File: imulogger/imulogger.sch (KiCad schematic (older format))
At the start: 23 parts, among them J1 DEBUG, J2 BATCONN, J3 CHGCONN, J4 Micro_SD_Card, SW1 SW_SPDT, U1 ESP32-WROOM-32, U2 USFS, U3 MCP1826S

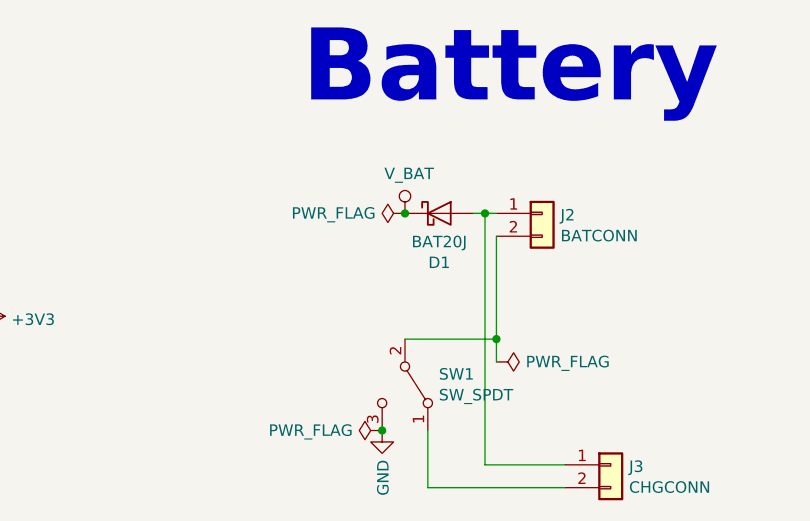
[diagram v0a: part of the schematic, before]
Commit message: make switch route V_BAT instead of GND
even though it shouldn't make a difference it's probably better to
not connect the system load to the charger.
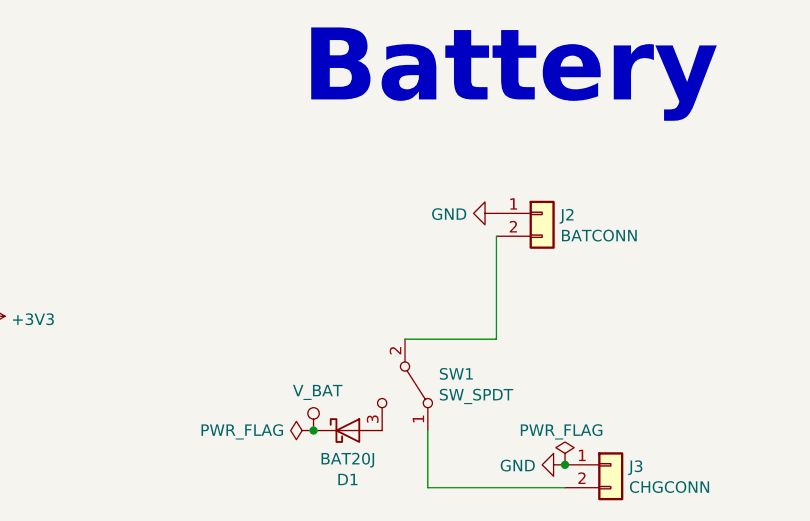
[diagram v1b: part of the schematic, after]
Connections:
- net GND: now also J2.1 (Pin_1), J3.1 (Pin_1); no longer SW1.3 (C)
- new net: D1.2 (A), SW1.3 (C)
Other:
- moved on the sheet: D1
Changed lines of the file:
@@
 $EndComp
-$Comp
-L imulogger-symbols:V_BAT #PWR014
-U 1 1 5CDD3FAE
-P 4350 6450
-F 0 "#PWR014" H 4350 6300 50  0001 C CNN
-F 1 "V_BAT" H 4368 6623 50  0000 C CNN
-F 2 "" H 4350 6450 50  0001 C CNN
-F 3 "" H 4350 6450 50  0001 C CNN
-	1    4350 6450
-	1    0    0    -1
-$EndComp
-Wire Wire Line
-	4750 6550 4750 7000
 $Comp
 L power:GND #PWR013
 U 1 1 5CDF671F
-P 4250 7400
-F 0 "#PWR013" H 4250 7150 50  0001 C CNN
-F 1 "GND" V 4255 7272 50  0000 R CNN
-F 2 "" H 4250 7400 50  0001 C CNN
-F 3 "" H 4250 7400 50  0001 C CNN
-	1    4250 7400
-	1    0    0    -1
-$EndComp
-$Comp
-L power:PWR_FLAG #FLG0105
-U 1 1 5CE03E12
-P 4750 7100
-F 0 "#FLG0105" H 4750 7175 50  0001 C CNN
-F 1 "PWR_FLAG" V 4750 7228 50  0000 L CNN
-F 2 "" H 4750 7100 50  0001 C CNN
-F 3 "~" H 4750 7100 50  0001 C CNN
-	1    4750 7100
+P 4750 6450
+F 0 "#PWR013" H 4750 6200 50  0001 C CNN
+F 1 "GND" V 4755 6322 50  0000 R CNN
+F 2 "" H 4750 6450 50  0001 C CNN
+F 3 "" H 4750 6450 50  0001 C CNN
+	1    4750 6450
 	0    1    1    0
 $EndComp
@@
 L Device:D_Schottky D1
 U 1 1 5CE2A47D
-P 4500 6450
-F 0 "D1" H 4500 6234 50  0000 C CNN
-F 1 "BAT20J" H 4500 6325 50  0000 C CNN
-F 2 "Diode_SMD:D_SOD-323" H 4500 6450 50  0001 C CNN
-F 3 "~" H 4500 6450 50  0001 C CNN
-	1    4500 6450
+P 4100 7400
+F 0 "D1" H 4100 7184 50  0000 C CNN
+F 1 "BAT20J" H 4100 7275 50  0000 C CNN
+F 2 "Diode_SMD:D_SOD-323" H 4100 7400 50  0001 C CNN
+F 3 "~" H 4100 7400 50  0001 C CNN
+	1    4100 7400
 	1    0    0    -1
 $EndComp
@@
 Wire Wire Line
 	4350 7000 4750 7000
-Connection ~ 4750 7000
-Wire Wire Line
-	4750 7000 4750 7100
 $Comp
 L Connector_Generic:Conn_01x02 J3
@@
 Wire Wire Line
 	4450 7650 4450 7400
-Wire Wire Line
-	4650 6450 4700 6450
-Wire Wire Line
-	5050 7550 4700 7550
-Wire Wire Line
-	4700 7550 4700 6450
-Connection ~ 4700 6450
-Wire Wire Line
-	4700 6450 4750 6450
 Text Notes 3900 6000 0    315  ~ 63
 Battery
 $Comp
-L power:PWR_FLAG #FLG0101
-U 1 1 5CE43E5A
-P 4350 6450
-F 0 "#FLG0101" H 4350 6525 50  0001 C CNN
-F 1 "PWR_FLAG" V 4350 6578 50  0000 L CNN
-F 2 "" H 4350 6450 50  0001 C CNN
-F 3 "~" H 4350 6450 50  0001 C CNN
-	1    4350 6450
-	0    -1   -1   0
+L imulogger-symbols:V_BAT #PWR014
+U 1 1 5CDD3FAE
+P 3950 7400
+F 0 "#PWR014" H 3950 7250 50  0001 C CNN
+F 1 "V_BAT" H 3968 7573 50  0000 C CNN
+F 2 "" H 3950 7400 50  0001 C CNN
+F 3 "" H 3950 7400 50  0001 C CNN
+	1    3950 7400
+	1    0    0    -1
 $EndComp
-Connection ~ 4350 6450
+Wire Wire Line
+	4750 6550 4750 7000
+$Comp
+L power:GND #PWR0105
+U 1 1 5CE55355
+P 5050 7550
+F 0 "#PWR0105" H 5050 7300 50  0001 C CNN
+F 1 "GND" V 5055 7422 50  0000 R CNN
+F 2 "" H 5050 7550 50  0001 C CNN
+F 3 "" H 5050 7550 50  0001 C CNN
+	1    5050 7550
+	0    1    1    0
+$EndComp
 $Comp
 L power:PWR_FLAG #FLG0102
 U 1 1 5CE450C6
-P 4250 7400
-F 0 "#FLG0102" H 4250 7475 50  0001 C CNN
-F 1 "PWR_FLAG" V 4250 7528 50  0000 L CNN
-F 2 "" H 4250 7400 50  0001 C CNN
-F 3 "~" H 4250 7400 50  0001 C CNN
-	1    4250 7400
+P 3950 7400
+F 0 "#FLG0102" H 3950 7475 50  0001 C CNN
+F 1 "PWR_FLAG" V 3950 7528 50  0000 L CNN
+F 2 "" H 3950 7400 50  0001 C CNN
+F 3 "~" H 3950 7400 50  0001 C CNN
+	1    3950 7400
 	0    -1   -1   0
 $EndComp
-Connection ~ 4250 7400
+Connection ~ 3950 7400
+$Comp
+L power:PWR_FLAG #FLG0101
+U 1 1 5CE59437
+P 5050 7550
+F 0 "#FLG0101" H 5050 7625 50  0001 C CNN
+F 1 "PWR_FLAG" H 4850 7700 50  0000 L CNN
+F 2 "" H 5050 7550 50  0001 C CNN
+F 3 "~" H 5050 7550 50  0001 C CNN
+	1    5050 7550
+	1    0    0    -1
+$EndComp
+Connection ~ 5050 7550
 $EndSCHEMATC

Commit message: properly separate i2c and sd using ground plane
unfortunately I had to remove the 3V3 pin to achieve this
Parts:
- J1: footprint Connector_PinHeader_2.54mm:PinHeader_1x06_P2.54mm_Vertical -> Connector_PinHeader_2.54mm:PinHeader_1x05_P2.54mm_Vertical; symbol Connector_Generic:Conn_01x06 -> Connector_Generic:Conn_01x05
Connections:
- net GND: now also J1.5 (Pin_5); no longer J1.6 (Pin_6)
- net IO0: now also J1.4 (Pin_4); no longer J1.5 (Pin_5)
- no-connect marks 30 -> 29
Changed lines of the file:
@@
 $EndComp
 $Comp
-L Connector_Generic:Conn_01x06 J1
+L Connector_Generic:Conn_01x05 J1
 U 1 1 5CB859D4
 P 5050 1900
 F 0 "J1" H 5130 1892 50  0000 L CNN
 F 1 "DEBUG" H 5130 1801 50  0000 L CNN
-F 2 "Connector_PinHeader_2.54mm:PinHeader_1x06_P2.54mm_Vertical" H 5050 1900 50  0001 C CNN
+F 2 "Connector_PinHeader_2.54mm:PinHeader_1x05_P2.54mm_Vertical" H 5050 1900 50  0001 C CNN
 F 3 "~" H 5050 1900 50  0001 C CNN
 	1    5050 1900
@@
 Text GLabel 4850 1900 0    50   Input ~ 0
 RXD0
-Text GLabel 4850 2100 0    50   Input ~ 0
+Text GLabel 4850 2000 0    50   Input ~ 0
 IO0
 $Comp
 L power:GND #PWR0106
 U 1 1 5CB87E5F
-P 4850 2200
-F 0 "#PWR0106" H 4850 1950 50  0001 C CNN
-F 1 "GND" V 4855 2072 50  0000 R CNN
-F 2 "" H 4850 2200 50  0001 C CNN
-F 3 "" H 4850 2200 50  0001 C CNN
-	1    4850 2200
+P 4850 2100
+F 0 "#PWR0106" H 4850 1850 50  0001 C CNN
+F 1 "GND" V 4855 1972 50  0000 R CNN
+F 2 "" H 4850 2100 50  0001 C CNN
+F 3 "" H 4850 2100 50  0001 C CNN
+	1    4850 2100
 	0    1    1    0
 $EndComp
@@
 	1    0    0    -1
 $EndComp
-NoConn ~ 4850 2000
 Wire Wire Line
 	2000 6900 2500 6900
